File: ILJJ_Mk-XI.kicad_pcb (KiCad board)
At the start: 2 copper layers, 124.5 x 96.5 mm, 83 parts, among them J0 Conn_02x12_Odd_Even, J1 Conn_02x12_Odd_Even, J2 Conn_02x12_Odd_Even, J3 Conn_02x12_Odd_Even, J4 Conn_02x12_Odd_Even, J5 Conn_02x12_Odd_Even, SW0 SW_Coded_SH-7070, SW1 SW_Coded_SH-7070, SW2 SW_Coded_SH-7070, SW3 SW_Coded_SH-7070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

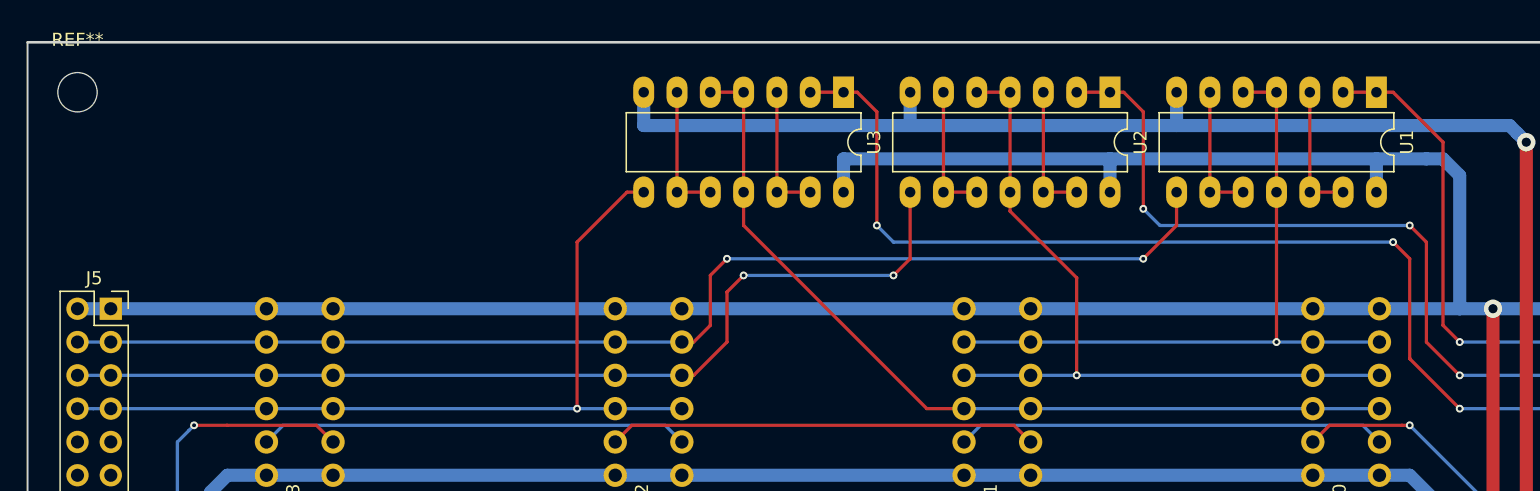
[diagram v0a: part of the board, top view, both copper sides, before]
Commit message: [change] バッファの配線を変更
まあ元の配線がどう考えてもおかしい
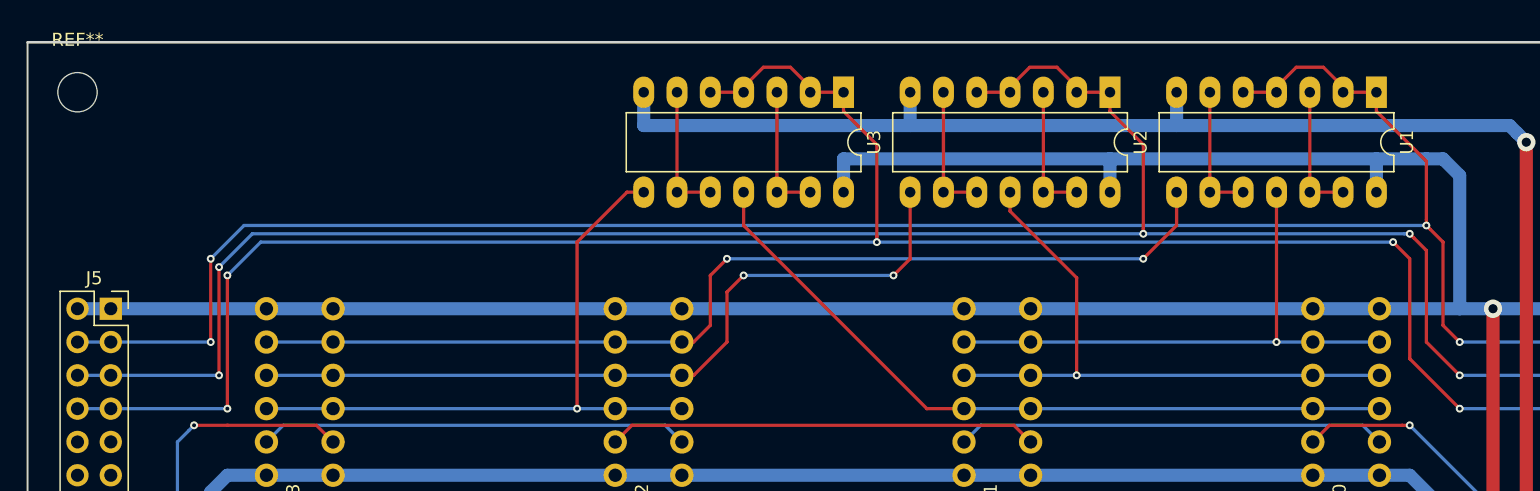
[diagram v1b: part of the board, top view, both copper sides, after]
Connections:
- J5 pad 3: /F2_2 -> /F2
- J5 pad 4: /F2_2 -> /F2
- J5 pad 5: /F1_2 -> /F1
- J5 pad 6: /F1_2 -> /F1
- J5 pad 7: /F0_2 -> /F0
- J5 pad 8: /F0_2 -> /F0
- U1 pad 4: /F2_1 -> /F2
- U1 pad 5: /F2_1 -> /F2
- U2 pad 4: /F1_1 -> /F1
- U2 pad 5: /F1_1 -> /F1
- U3 pad 4: /F0_1 -> /F0
- U3 pad 5: /F0_1 -> /F0
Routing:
- net /F2: track 36.4 -> 155.6 mm, vias 1 -> 4
- net /F1: track 58.4 -> 158.8 mm, vias 3 -> 5
- net /F0: track 80.5 -> 162.5 mm, vias 3 -> 5
- net /F2_2: track 92.3 -> 77.9 mm
- net /F1_2: track 74.5 -> 60.1 mm
- net /F0_2: track 65.4 -> 51.0 mm
- net /F0_1: track 67.0 -> 56.8 mm
- net /F1_1: track 57.9 -> 47.8 mm
- net /F2_1: track 53.3 -> 43.1 mm

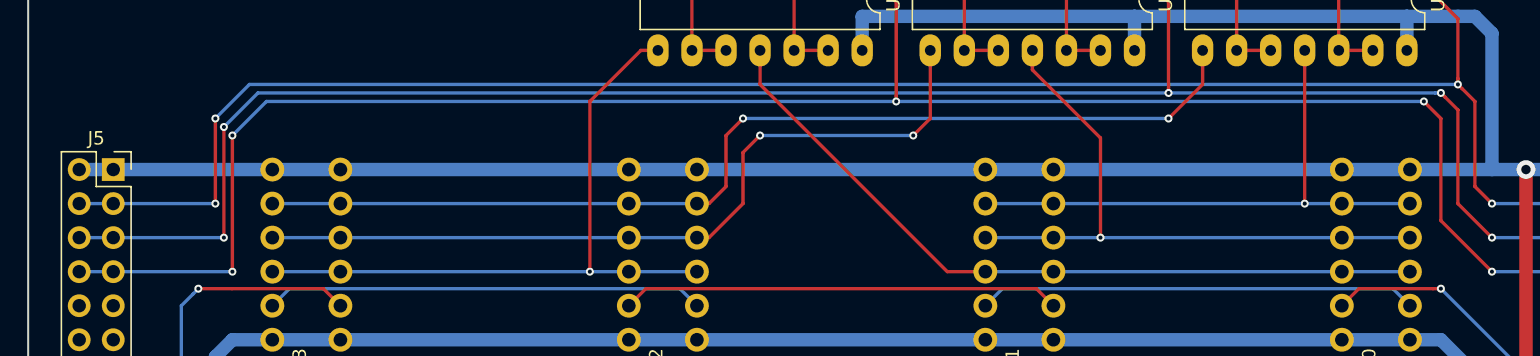
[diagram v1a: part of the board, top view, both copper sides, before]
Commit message: [clean] 配線のちょっとした調整
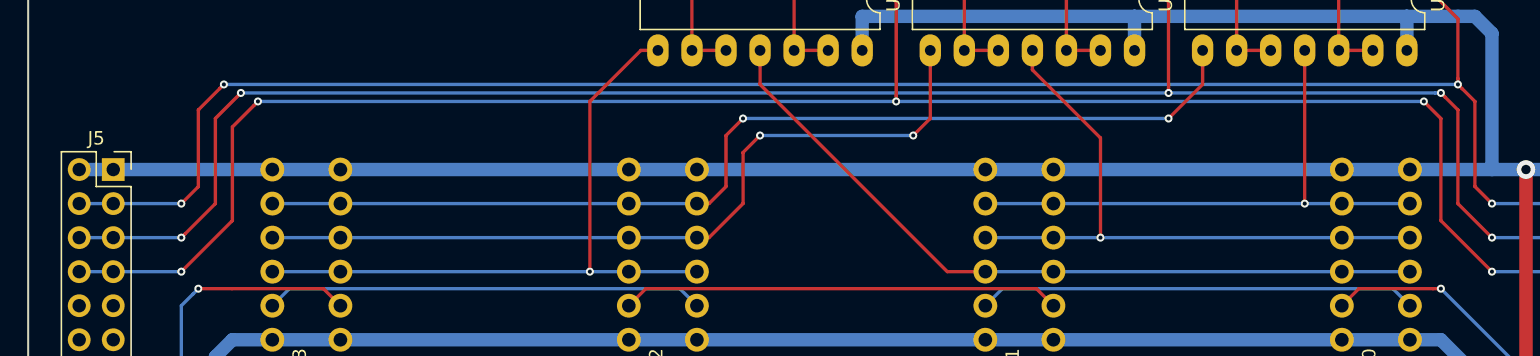
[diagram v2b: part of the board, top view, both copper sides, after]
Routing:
- net /F0: track 162.5 -> 160.6 mm
- net /F1: track 158.8 -> 157.6 mm
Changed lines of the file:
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@@
     (thickness 1.6)
     (drawings 4)
-    (tracks 618)
+    (tracks 625)
     (zones 0)
     (modules 83)
@@
   (segment (start 163.83 54.79) (end 166.37 57.33) (width 0.25) (layer F.Cu) (net 99))
   (segment (start 166.37 64.345736) (end 166.37 64.77) (width 0.25) (layer F.Cu) (net 99))
-  (via (at 116.84 67.31) (size 0.6) (drill 0.3) (layers F.Cu B.Cu) (net 99))
-  (segment (start 119.38 64.77) (end 116.84 67.31) (width 0.25) (layer B.Cu) (net 99))
-  (segment (start 166.37 64.77) (end 119.38 64.77) (width 0.25) (layer B.Cu) (net 99))
-  (via (at 116.84 77.47) (size 0.6) (drill 0.3) (layers F.Cu B.Cu) (net 99))
-  (segment (start 116.84 67.31) (end 116.84 77.47) (width 0.25) (layer F.Cu) (net 99))
-  (segment (start 116.84 77.47) (end 105.41 77.47) (width 0.25) (layer B.Cu) (net 99))
+  (segment (start 105.41 77.47) (end 113.03 77.47) (width 0.25) (layer B.Cu) (net 99))
+  (via (at 113.03 77.47) (size 0.6) (drill 0.3) (layers F.Cu B.Cu) (net 99))
+  (via (at 118.745 64.77) (size 0.6) (drill 0.3) (layers F.Cu B.Cu) (net 99))
+  (segment (start 166.37 64.77) (end 118.745 64.77) (width 0.25) (layer B.Cu) (net 99))
+  (segment (start 118.445001 65.069999) (end 118.745 64.77) (width 0.25) (layer F.Cu) (net 99))
+  (segment (start 116.84 66.675) (end 118.445001 65.069999) (width 0.25) (layer F.Cu) (net 99))
+  (segment (start 116.84 73.66) (end 116.84 66.675) (width 0.25) (layer F.Cu) (net 99))
+  (segment (start 113.03 77.47) (end 116.84 73.66) (width 0.25) (layer F.Cu) (net 99))
   (via (at 210.82 74.93) (size 0.6) (drill 0.3) (layers F.Cu B.Cu) (net 100))
   (segment (start 219.71 74.93) (end 210.82 74.93) (width 0.25) (layer B.Cu) (net 100) (status 10))
@@
   (segment (start 184.15 53.34) (end 184.15 54.79) (width 0.25) (layer F.Cu) (net 100))
   (via (at 186.69 64.135) (size 0.6) (drill 0.3) (layers F.Cu B.Cu) (net 100))
-  (via (at 116.205 66.675) (size 0.6) (drill 0.3) (layers F.Cu B.Cu) (net 100))
-  (segment (start 118.745 64.135) (end 116.205 66.675) (width 0.25) (layer B.Cu) (net 100))
-  (segment (start 186.69 64.135) (end 118.745 64.135) (width 0.25) (layer B.Cu) (net 100))
-  (via (at 116.205 74.93) (size 0.6) (drill 0.3) (layers F.Cu B.Cu) (net 100))
-  (segment (start 116.205 66.675) (end 116.205 74.93) (width 0.25) (layer F.Cu) (net 100))
-  (segment (start 116.205 74.93) (end 105.41 74.93) (width 0.25) (layer B.Cu) (net 100))
+  (via (at 117.475 64.13499) (size 0.6) (drill 0.3) (layers F.Cu B.Cu) (net 100))
+  (segment (start 186.69 64.135) (end 117.47501 64.135) (width 0.25) (layer B.Cu) (net 100))
+  (segment (start 117.47501 64.135) (end 117.475 64.13499) (width 0.25) (layer B.Cu) (net 100))
+  (segment (start 105.41 74.93) (end 113.03 74.93) (width 0.25) (layer B.Cu) (net 100))
+  (via (at 113.03 74.93) (size 0.6) (drill 0.3) (layers F.Cu B.Cu) (net 100))
+  (segment (start 113.329999 74.630001) (end 113.03 74.93) (width 0.25) (layer F.Cu) (net 100))
+  (segment (start 115.57 72.39) (end 113.329999 74.630001) (width 0.25) (layer F.Cu) (net 100))
+  (segment (start 115.57 66.03999) (end 115.57 72.39) (width 0.25) (layer F.Cu) (net 100))
+  (segment (start 117.475 64.13499) (end 115.57 66.03999) (width 0.25) (layer F.Cu) (net 100))
   (via (at 210.82 72.39) (size 0.6) (drill 0.3) (layers F.Cu B.Cu) (net 101))
   (segment (start 219.71 72.39) (end 210.82 72.39) (width 0.25) (layer B.Cu) (net 101) (status 10))
@@
   (segment (start 209.55 71.12) (end 209.55 64.77) (width 0.25) (layer F.Cu) (net 101))
   (segment (start 210.82 72.39) (end 209.55 71.12) (width 0.25) (layer F.Cu) (net 101))
-  (via (at 115.57 66.04) (size 0.6) (drill 0.3) (layers F.Cu B.Cu) (net 101))
-  (segment (start 118.11 63.5) (end 115.57 66.04) (width 0.25) (layer B.Cu) (net 101))
-  (segment (start 208.28 63.5) (end 118.11 63.5) (width 0.25) (layer B.Cu) (net 101))
-  (via (at 115.57 72.39) (size 0.6) (drill 0.3) (layers F.Cu B.Cu) (net 101))
-  (segment (start 115.57 66.04) (end 115.57 72.39) (width 0.25) (layer F.Cu) (net 101))
-  (segment (start 115.57 72.39) (end 105.41 72.39) (width 0.25) (layer B.Cu) (net 101))
+  (via (at 113.03 72.39) (size 0.6) (drill 0.3) (layers F.Cu B.Cu) (net 101))
+  (segment (start 105.41 72.39) (end 113.03 72.39) (width 0.25) (layer B.Cu) (net 101))
+  (segment (start 208.28 63.5) (end 116.205008 63.5) (width 0.25) (layer B.Cu) (net 101))
+  (via (at 116.205008 63.5) (size 0.6) (drill 0.3) (layers F.Cu B.Cu) (net 101))
+  (segment (start 114.3 65.405008) (end 115.905009 63.799999) (width 0.25) (layer F.Cu) (net 101))
+  (segment (start 114.3 71.12) (end 114.3 65.405008) (width 0.25) (layer F.Cu) (net 101))
+  (segment (start 115.905009 63.799999) (end 116.205008 63.5) (width 0.25) (layer F.Cu) (net 101))
+  (segment (start 113.03 72.39) (end 114.3 71.12) (width 0.25) (layer F.Cu) (net 101))
   (segment (start 191.77 53.34) (end 191.77 60.96) (width 0.25) (layer F.Cu) (net 114) (status 30))
   (segment (start 194.31 60.96) (end 191.77 60.96) (width 0.25) (layer F.Cu) (net 114) (status 30))

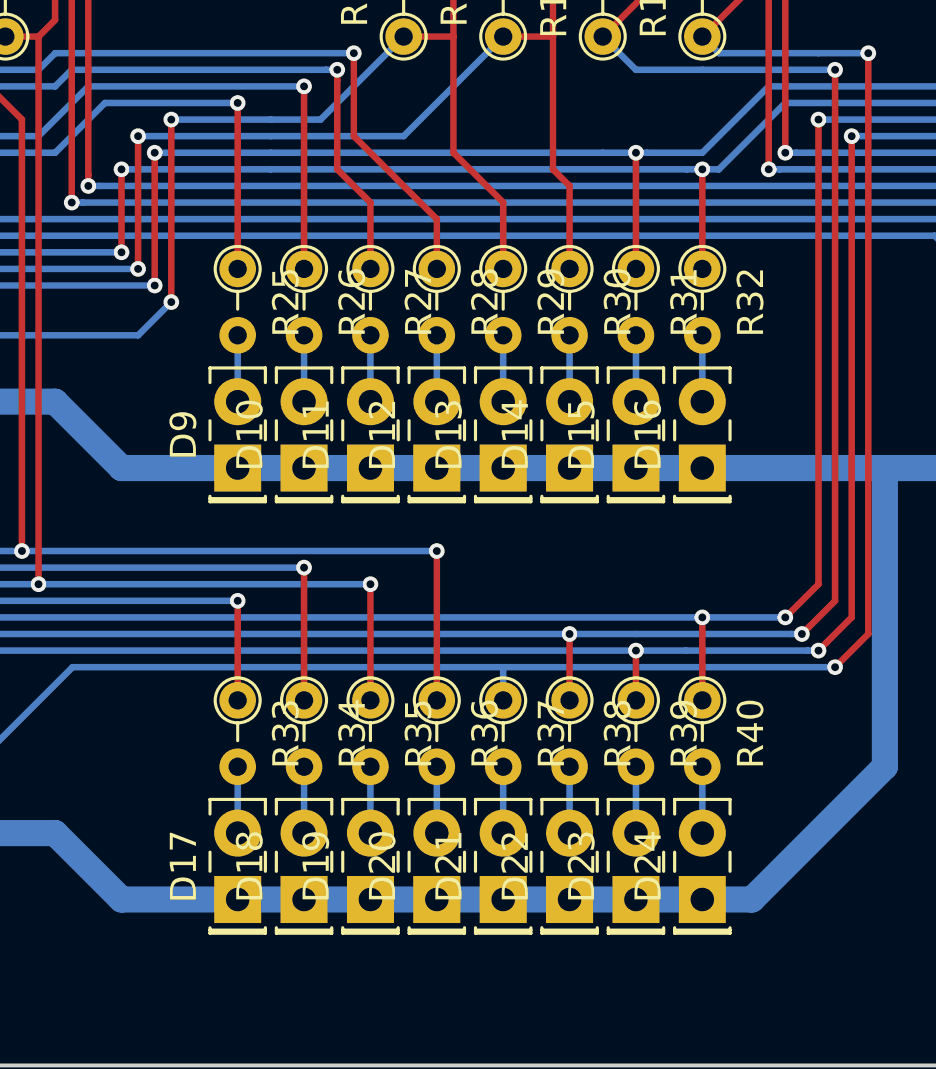
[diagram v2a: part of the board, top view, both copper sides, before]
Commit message: [clean] アノテーション印刷の位置を調整
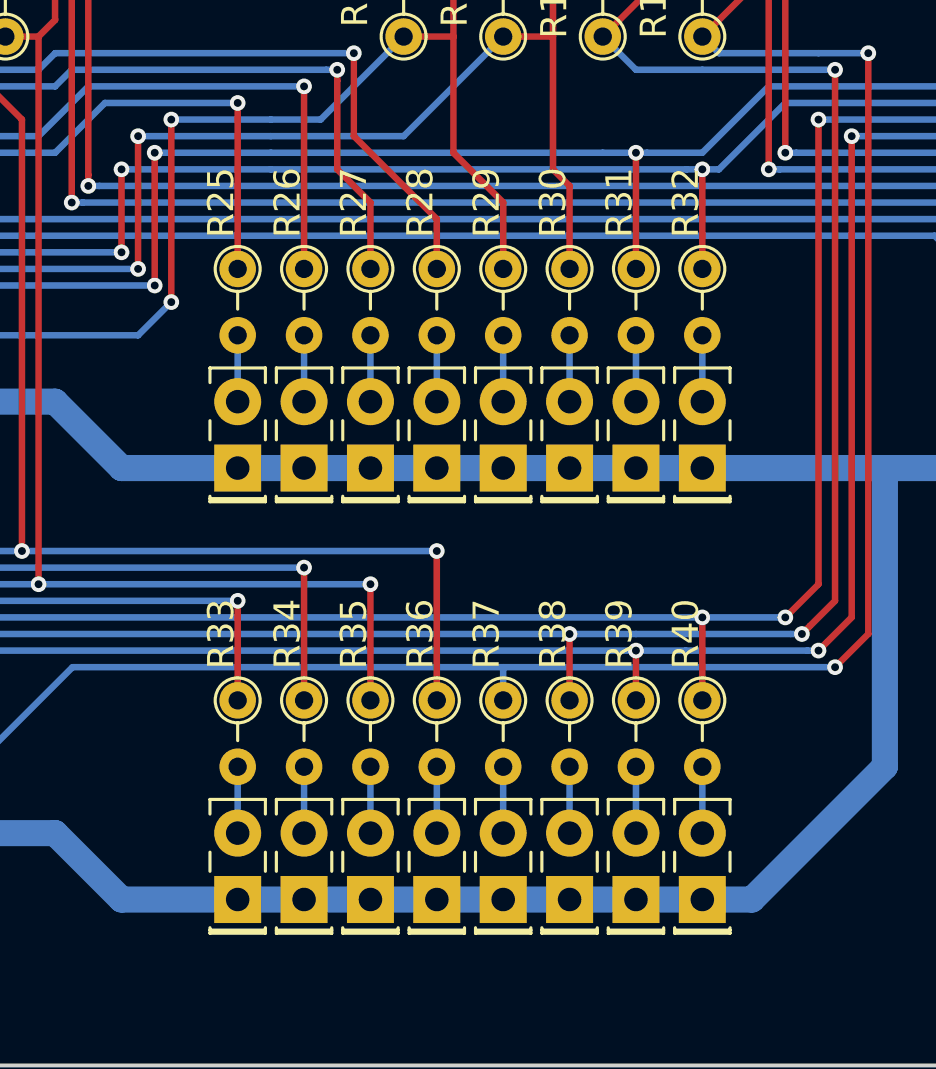
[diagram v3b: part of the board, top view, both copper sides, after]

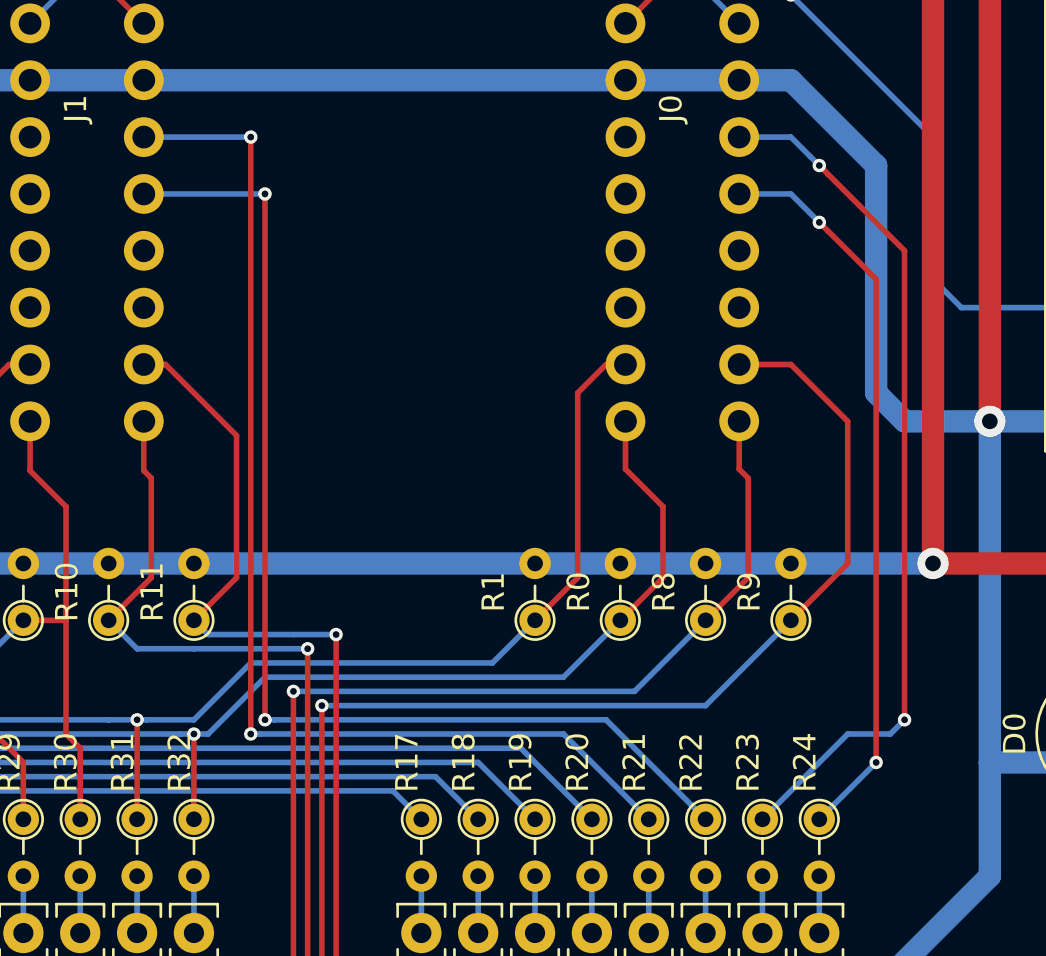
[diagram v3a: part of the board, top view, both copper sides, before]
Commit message: [clean] 配線をちょっと修正
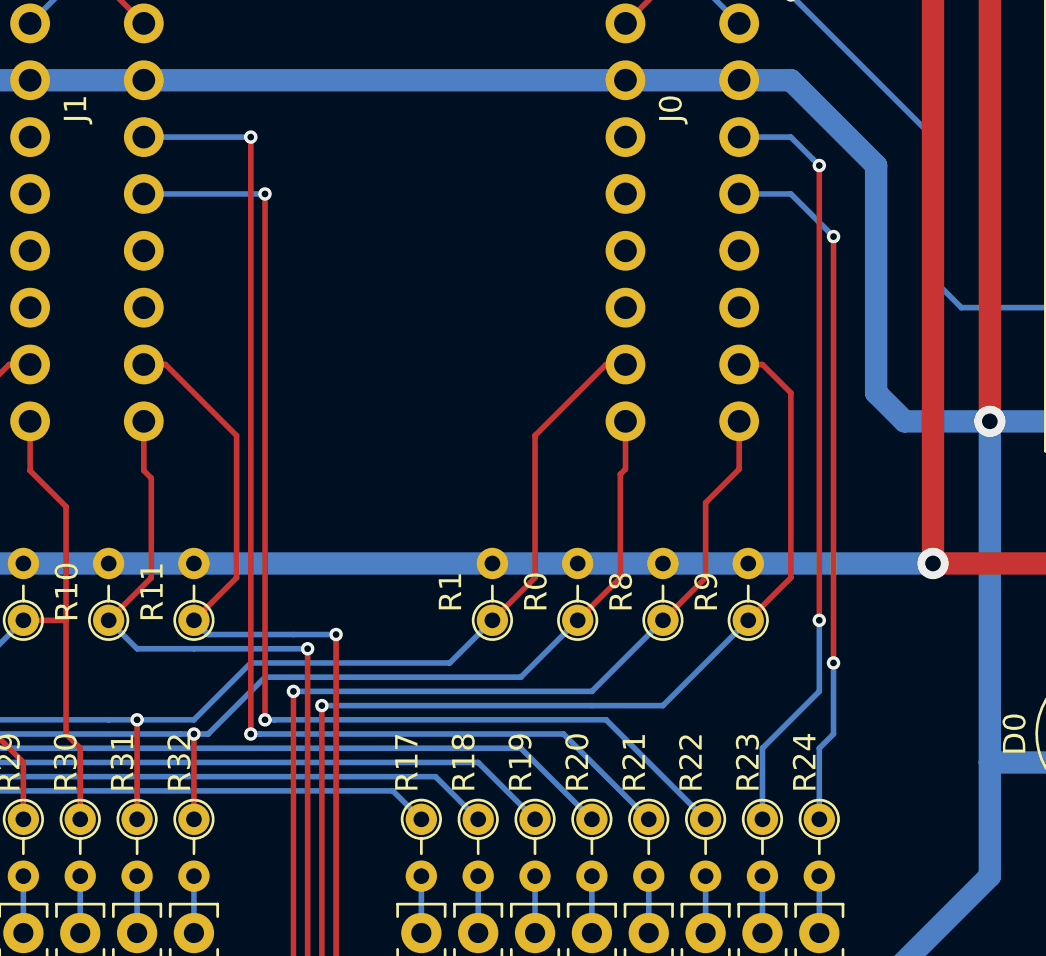
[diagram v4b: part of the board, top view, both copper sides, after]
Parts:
- moved R1 1.91 mm to (193.7, 106.7)
- moved R8 1.91 mm to (201.3, 106.7)
- moved R9 1.91 mm to (205.1, 106.7)
- moved R0 1.90 mm to (197.5, 106.7)
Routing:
- net /S1: track 38.6 -> 34.4 mm
- net /B1: track 105.8 -> 101.8 mm
- net /A0: track 77.4 -> 74.9 mm
- net /S0: track 32.9 -> 31.3 mm
- net /B0: track 95.4 -> 94.0 mm
- net /A1: track 80.0 -> 78.9 mm
